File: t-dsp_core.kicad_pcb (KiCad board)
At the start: 4 copper layers, 100 x 61 mm, 165 parts, among them IC1 Logic Level Shifter - 74HCT2G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, J1 J_PWR, J10 J_DMX, J11 J_LED, J12 J_ETH, J13 u.FL DNP (IDC767 ext-antenna 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, J2 J_TDM, J3 J_T, J4 J_USBH, J5 J_MIDI, J6 J_SPDIF, J7 J_AUX, J8 J_S3, J9 J_USB3, T108 Tab, T109 Tab, T110 Tab, T111 Tab, U1 Teensy 4.1 - DEVKIT, U11 Dual Buffer - SN74LVC2G125DCTR, U13 ESP32-S3-WROOM-1-N16R8, U15 LT3045EMSE#TRPBF, U16 THVD1450DR, U17 ISO7762DW, U18 TEA1-0505HI, U19 SRC4382IPFBR, U20 TLV75718PDRVR, U21 74LVC157APW, U22 IDC777-1, U23 74LVC157APW, U24 AP63203WU, U3 Power Mux & Protect - TPS2116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, U4 Optoisolators - H11L1SM - 6-S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, U5 Dual Buffer - SN74LVC2G125DCTR, U6 Dual Buffer - SN74LVC2G125DCTR, U7 Dual Buffer - SN74LVC2G125DCTR, U8 Dual Buffer - SN74LVC2G125DCTR, U9 Dual Buffer - 74HCT2G17GW,125, Y1 24.576MHz

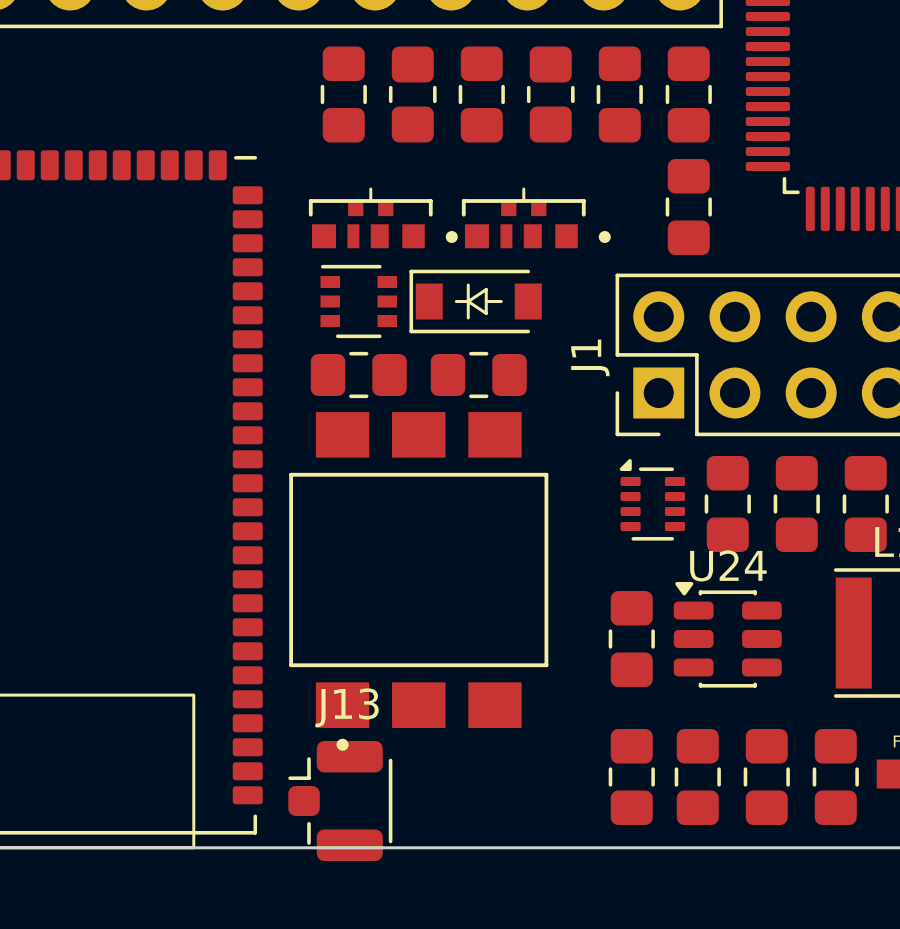
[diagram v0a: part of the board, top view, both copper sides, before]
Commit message: Spin 2 stage 10k: opto row stacked up to clear the u.FL courtyard
Co-Authored-By: Claude Fable 5.1 <noreply@anthropic.com>
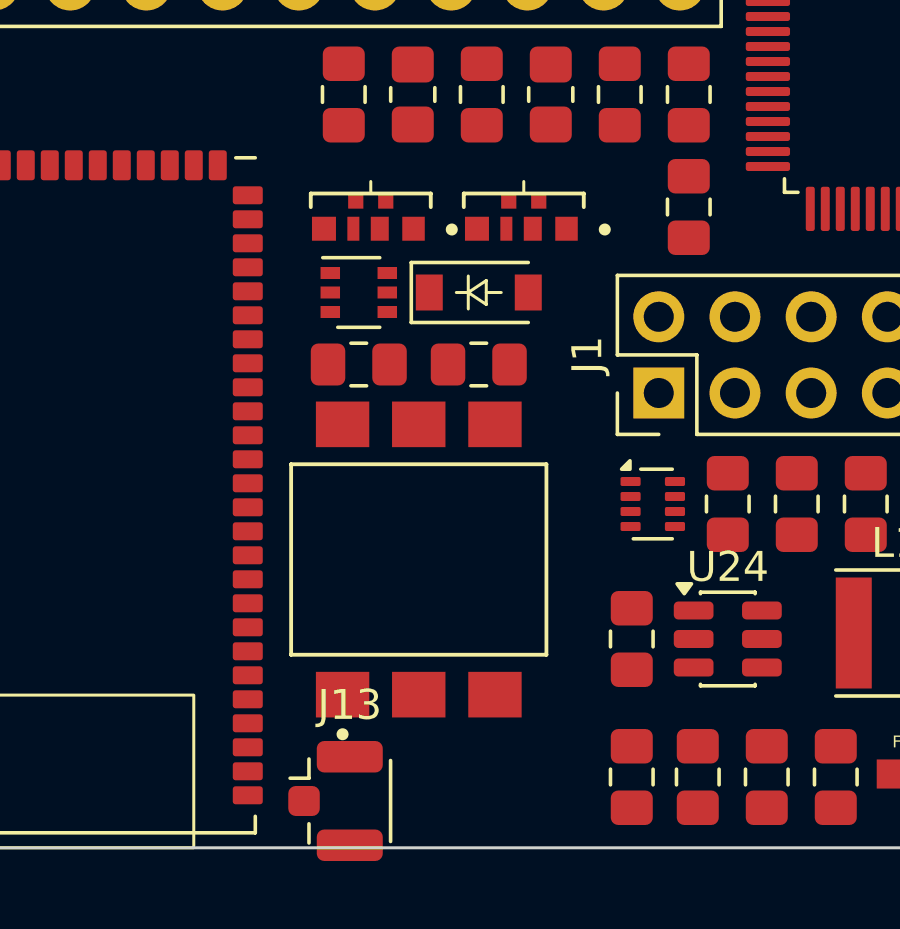
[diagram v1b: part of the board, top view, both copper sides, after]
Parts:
- moved C16 0.35 mm to (156.0, 183.9)
- moved C21 0.35 mm to (160.0, 183.9)
- moved U4 0.35 mm to (158.0, 190.4)
- moved D2 0.30 mm to (160.0, 181.5)
- moved U9 0.30 mm to (156.0, 181.5)
- moved D3 0.25 mm to (156.4, 178.2)
- moved D4 0.25 mm to (161.5, 178.2)
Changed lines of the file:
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@@
 	(footprint "project_fp:SOT-363_SC-70-6"
 		(layer "F.Cu")
-		(at 156 181.79)
+		(at 156 181.49)
 		(descr "SOT-363, SC-70-6")
 		(tags "SOT-363 SC-70-6")
@@
 	(footprint "project_fp:C_0805_2012Metric_Pad1.15x1.40mm_HandSolder"
 		(layer "F.Cu")
-		(at 160 184.24)
+		(at 160 183.89)
 		(descr "Capacitor SMD 0805 (2012 Metric), square (rectangular) end terminal, IPC_7351 nominal with elongated pad for handsoldering. (Body size source: https://docs.google.com/spreadsheets/d/1BsfQQcO9C6DZCsRaXUlFlo91Tg2WpOkGARC1WS5S8t0/edit?usp=sharing), generated with kicad-footprint-generator")
 		(tags "capacitor handsolder")
@@
 	(footprint "project_fp:IC_H11L1SM"
 		(layer "F.Cu")
-		(at 158 190.74 90)
+		(at 158 190.39 90)
 		(property "Reference" "U4"
 			(at -5.575 -4.15462 90)
@@
 	(footprint "project_fp:SK6812-32228SMD-Reverse-Mount_mod"
 		(layer "F.Cu")
-		(at 161.5 178.44)
+		(at 161.5 178.19)
 		(property "Reference" "D4"
 			(at -0.175 2.885 180)
@@
 	(footprint "project_fp:D_SOD-123"
 		(layer "F.Cu")
-		(at 160 181.79)
+		(at 160 181.49)
 		(descr "SOD-123")
 		(tags "SOD-123")
@@
 	(footprint "project_fp:SK6812-32228SMD-Reverse-Mount_mod"
 		(layer "F.Cu")
-		(at 156.4 178.44)
+		(at 156.4 178.19)
 		(property "Reference" "D3"
 			(at -0.175 2.885 180)
@@
 	(footprint "project_fp:C_0805_2012Metric_Pad1.15x1.40mm_HandSolder"
 		(layer "F.Cu")
-		(at 156 184.24)
+		(at 156 183.89)
 		(descr "Capacitor SMD 0805 (2012 Metric), square (rectangular) end terminal, IPC_7351 nominal with elongated pad for handsoldering. (Body size source: https://docs.google.com/spreadsheets/d/1BsfQQcO9C6DZCsRaXUlFlo91Tg2WpOkGARC1WS5S8t0/edit?usp=sharing), generated with kicad-footprint-generator")
 		(tags "capacitor handsolder")

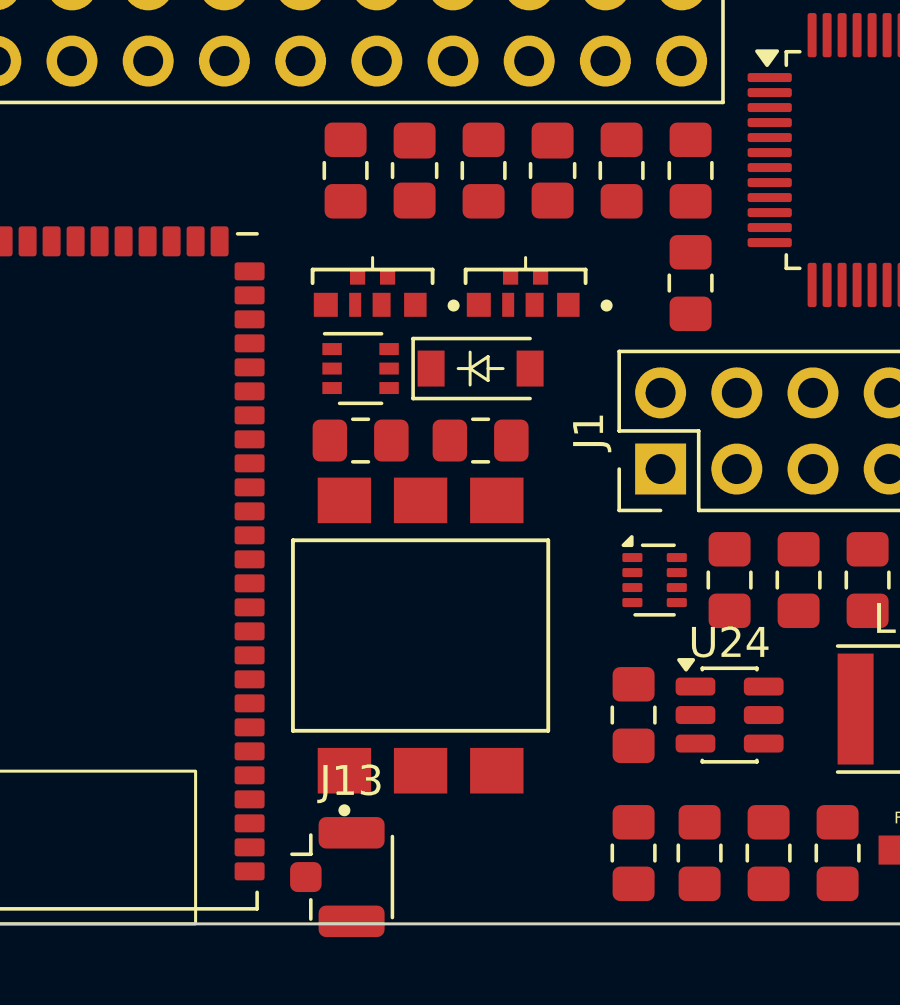
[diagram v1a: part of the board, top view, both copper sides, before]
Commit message: Spin 2 stage 10l: board re-synced (D3/D4 on the SK6812-EC20 land pattern, holes stay MountingHole_3.2mm_M3); U4 nudged 0.09 mm off R57
Co-Authored-By: Claude Fable 5.1 <noreply@anthropic.com>
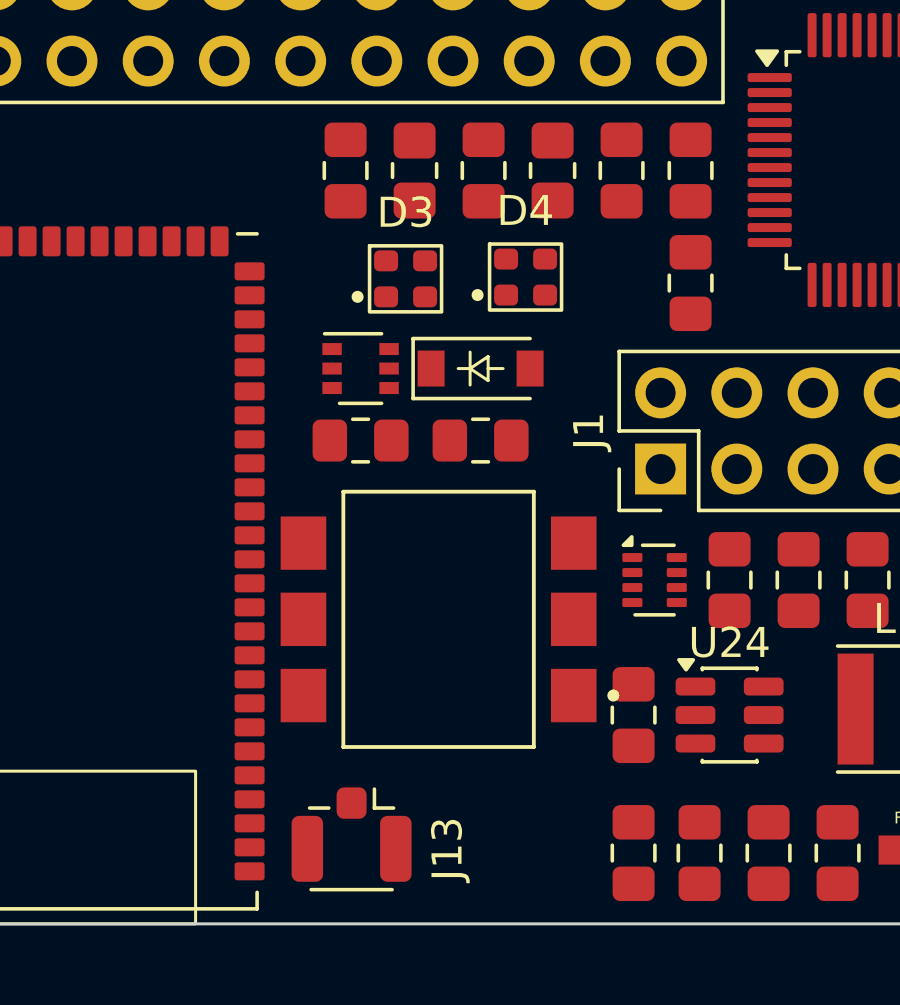
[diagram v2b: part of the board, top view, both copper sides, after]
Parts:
- D3, D4: value Side Light LED - SK6812 -> SK6812-EC20; footprint project_fp:SK6812-32228SMD-Reverse-Mount_mod -> project_fp:LED_SK6812-EC20_2.0x2.0mm
- moved D3 1.14 mm to (157.5, 178.5)
- moved J13 0.94 mm to (155.7, 197.5), turned to -90 degrees
- moved U4 0.81 mm to (158.6, 189.8), turned to 180 degrees
- moved D4 0.25 mm to (161.5, 178.4)

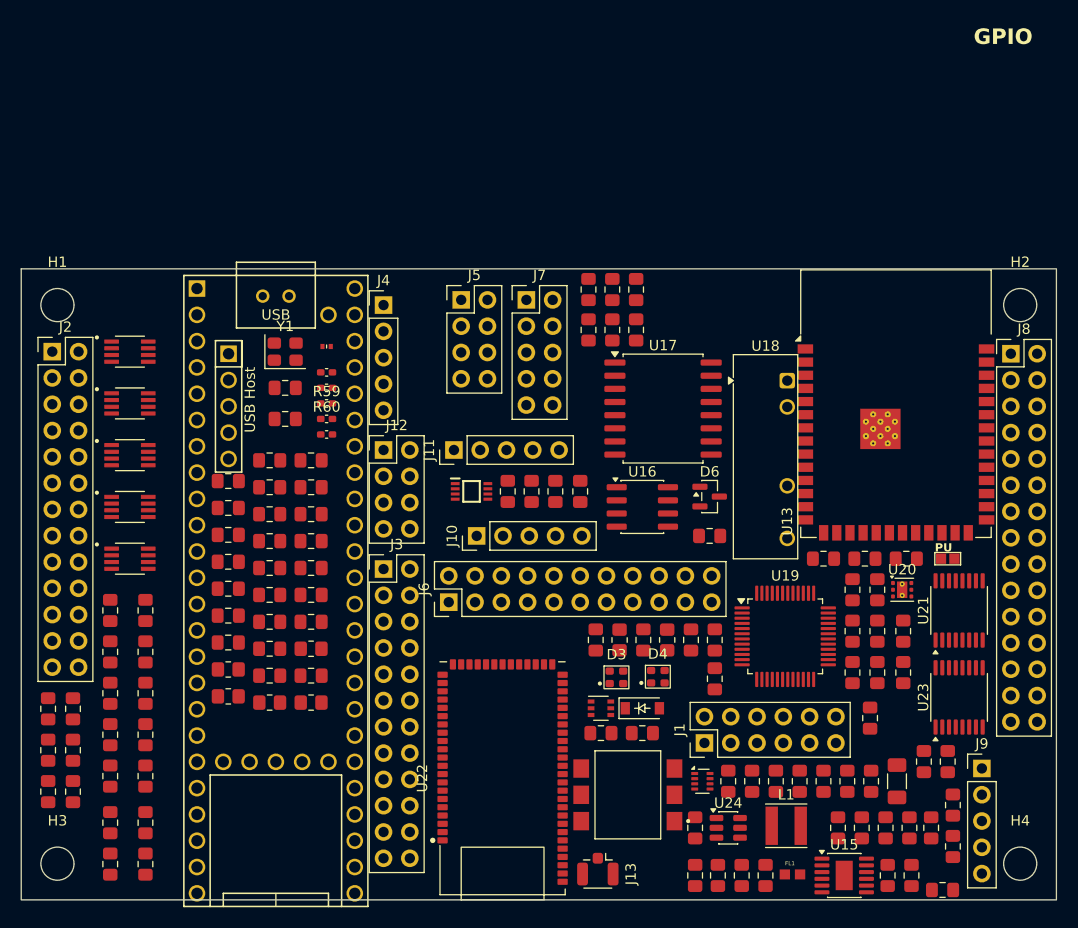
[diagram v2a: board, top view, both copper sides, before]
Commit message: Spin 2 stage 10m (1/2): board re-synced (J8 2x17, J1 2x5, J9 gone); chips, modules, headers and holes placed to the four-row / three-slot plan (change map 11.4) via pcbnew
Co-Authored-By: Claude Fable 5.1 <noreply@anthropic.com>
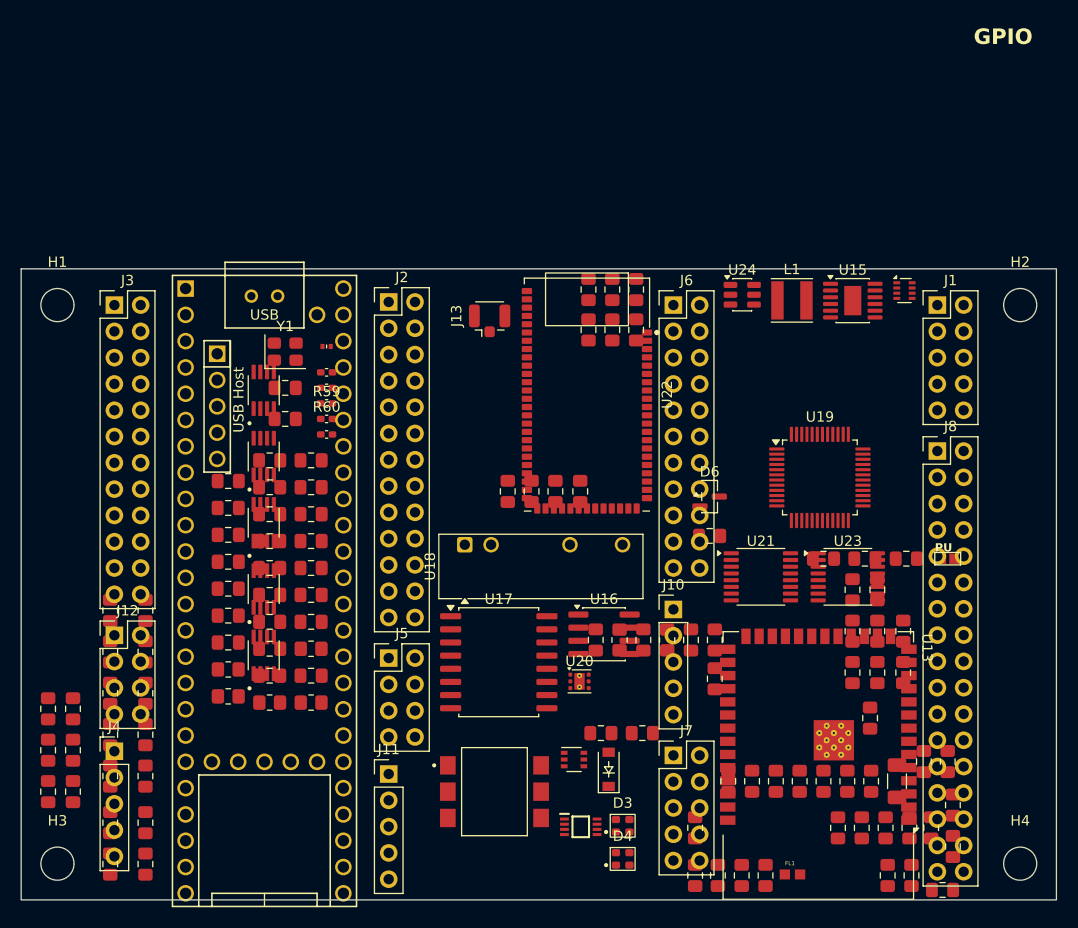
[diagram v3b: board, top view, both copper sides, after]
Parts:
- removed J9: J_USB3, Connector_PinHeader_2.54mm:PinHeader_1x05_P2.54mm_Vertical
- J1: footprint Connector_PinHeader_2.54mm:PinHeader_2x06_P2.54mm_Vertical -> Connector_PinHeader_2.54mm:PinHeader_2x05_P2.54mm_Vertical
- J8: footprint Connector_PinHeader_2.54mm:PinHeader_2x15_P2.54mm_Vertical -> Connector_PinHeader_2.54mm:PinHeader_2x17_P2.54mm_Vertical
- moved U15 55.5 mm to (180.3, 142.1)
- moved J13 54.9 mm to (145.2, 143.6), turned to 90 degrees
- moved U24 51.5 mm to (169.7, 141.5)
- moved U3 51.3 mm to (185.3, 141.1)
- moved L1 50.8 mm to (174.4, 142.1)
- moved J4 50.3 mm to (109.0, 185.6)
- moved J1 47.9 mm to (188.5, 142.5), turned to 0 degrees
- moved J7 46.2 mm to (163.0, 186.0)
- moved U22 37.9 mm to (154.7, 151.2), turned to -90 degrees
- moved J3 36.4 mm to (109.0, 142.5)
- moved J6 36.0 mm to (163.0, 142.5), turned to 0 degrees
- moved U13 35.8 mm to (177.0, 187.0), turned to 180 degrees
- moved J5 35.3 mm to (135.5, 176.6)
- moved U18 35.0 mm to (142.8, 165.7), turned to 90 degrees
- moved IC1 34.1 mm to (154.1, 192.9)
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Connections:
- J1 pad 10: 3.3V_DIG -> GND
- J1 pad 7: GND -> 3.3V
- J1 pad 8: GND -> 3.3V_DIG
- J1 pad 9: 3.3V -> V_BAT

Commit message: Spin 2 stage 10m (2/2): net-driven two-sided passive placement (caps front at the supply pins, 55 resistors/ferrites/diodes/jumper on the back under their pins), 4-layer stack (F.Cu, In1 GND, In2 PWR, B.Cu)
Placed with KiCad's pcbnew python on the saved file (the IPC path trips the project-lock dialog on 10.0.1).
Passive-to-pin: median 2.9 mm (was 9.9), 7 parts > 10 mm (was 59). DRC: no shorts/clearance; only the
stock ESP32 courtyard overlaps and the inherited drill warnings.

Co-Authored-By: Claude Fable 5.1 <noreply@anthropic.com>
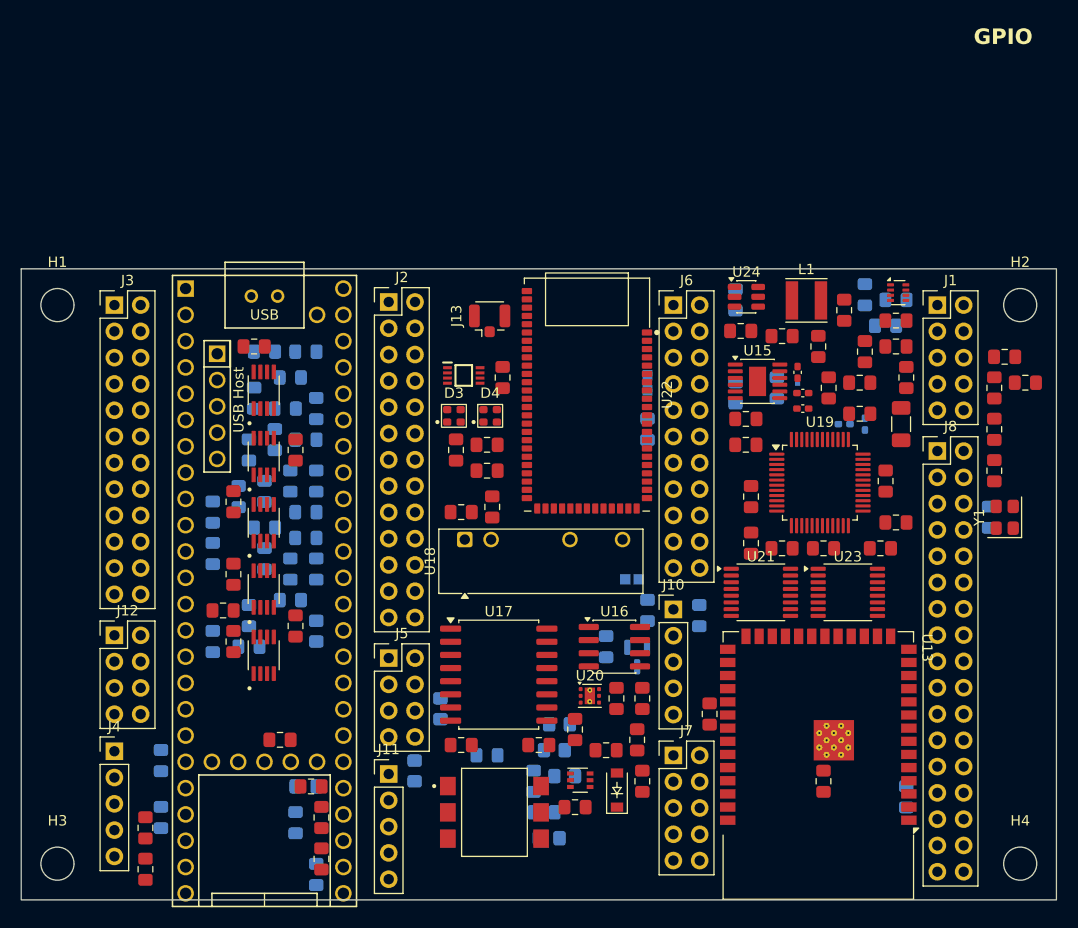
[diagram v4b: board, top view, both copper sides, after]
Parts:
- D6, FB1, FL1, PU_EN1, R1, R10, R11, R12, R13, R14, R15, R16, R17, R19, R2, R28, R29, R3, R30, R31, R32, R33, R34, R35, R36, R37, R38, R39, R4, R40, R41, R42, R43, R44, R45, R46, R47, R5, R52, R53, R54, R55, R56, R57, R58, R59, R6, R60, R61, R66, R67, R68, R7, R71, R72, R73, R8, R9: moved to B.Cu
- moved Y1 71.3 mm to (195.0, 163.0), turned to 90 degrees
- moved C44 69.0 mm to (194.0, 158.5), turned to -90 degrees
- moved R61 68.7 mm to (193.5, 163.0), turned to -90 degrees
- moved R72 65.6 mm to (160.5, 154.5)
- moved R30 58.0 mm to (181.5, 141.5), turned to -90 degrees
- moved C133 55.0 mm to (179.5, 143.0), turned to -90 degrees
- moved C33 53.1 mm to (112.0, 193.0)
- moved R66 53.0 mm to (169.0, 142.0)
- moved C1 52.2 mm to (112.0, 197.0), turned to -90 degrees
- moved R60 52.0 mm to (181.5, 154.0), turned to 90 degrees
- moved C131 51.4 mm to (169.5, 145.0), turned to 0 degrees
- moved R29 50.7 mm to (183.5, 144.5), turned to 0 degrees
- moved C29 50.3 mm to (145.0, 158.5), turned to 0 degrees
- moved R59 50.0 mm to (179.5, 154.0)
- moved FL1 49.5 mm to (160.5, 150.0), turned to 90 degrees
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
